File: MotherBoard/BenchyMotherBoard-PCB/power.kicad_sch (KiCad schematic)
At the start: 201 parts, among them J1 PWR-CONN, J4 UPDI-HEADER, U1 STM32MP157FAB1, U10 USB7206C, U2 TPS65400RGZT, U3 NCP51200, U4 ATTINY1606-MNR, U6 MAX15027, U7 SN74LVC1G32, U9 AP2127K-3.3

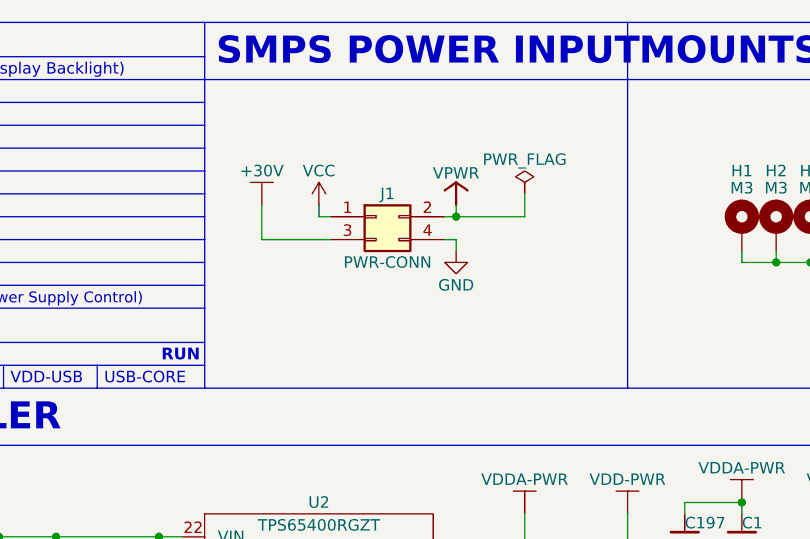
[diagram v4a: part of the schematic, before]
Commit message: Add extra functions to PMBus and create manual power sequence
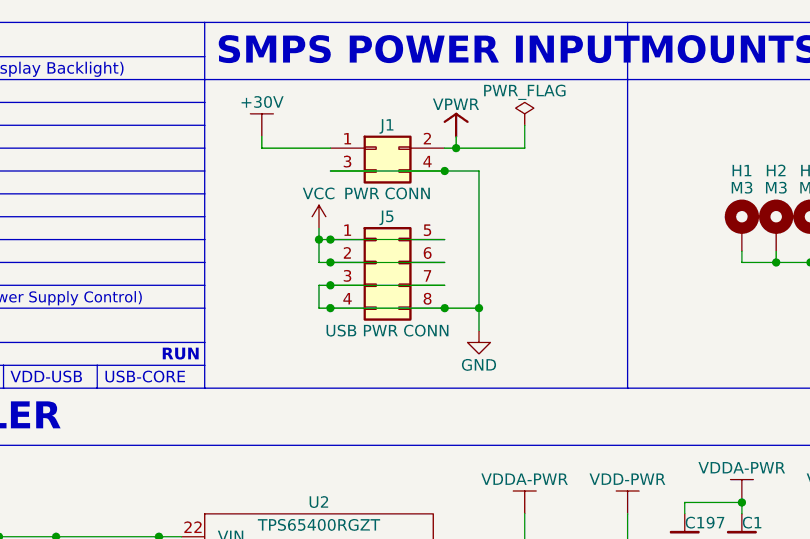
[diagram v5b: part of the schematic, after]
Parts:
- added J5: USB PWR CONN, Daxxn_Connectors:8-Pin_Molex_Mini-Fit_Jr_Vertical_Mount, symbol Connector_Generic:Conn_02x04_Top_Bottom
- J1: value PWR-CONN -> PWR CONN
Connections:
- net +30V: now also J1.1 (Pin_1); no longer J1.3 (Pin_3)
- net GND: now also J1.3 (Pin_3), J5.3 (Pin_3), J5.4 (Pin_4), J5.7 (Pin_7), J5.8 (Pin_8)
- net VCC: now also J5.1 (Pin_1), J5.2 (Pin_2), J5.5 (Pin_5), J5.6 (Pin_6); no longer J1.1 (Pin_1)
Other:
- moved on the sheet: J1

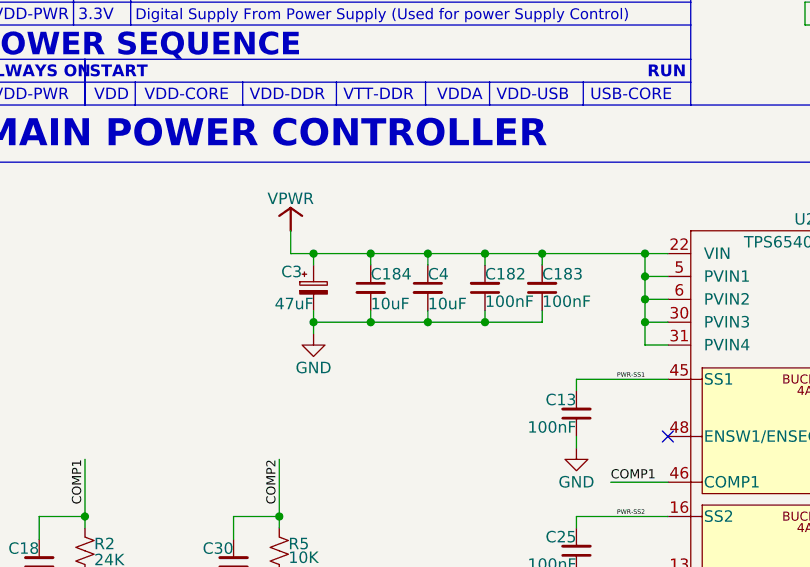
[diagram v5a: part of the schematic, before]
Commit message: Finish trace layout and update PS fb resistor values
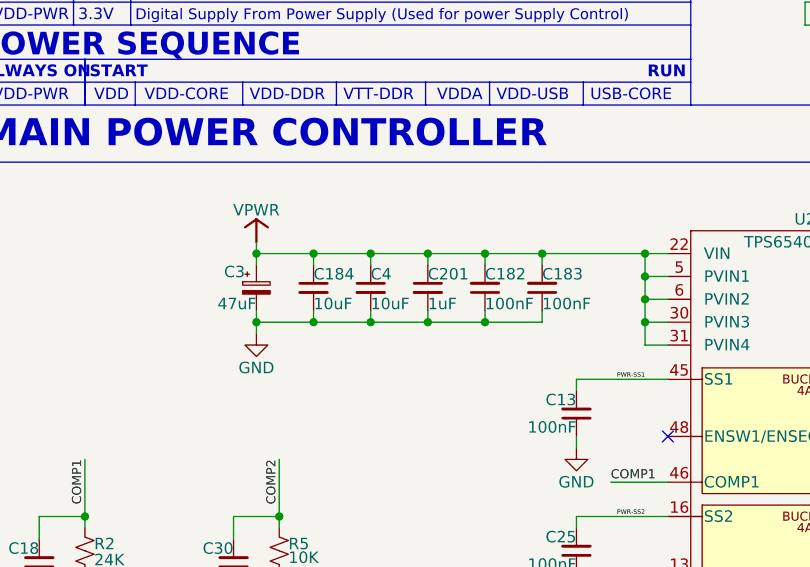
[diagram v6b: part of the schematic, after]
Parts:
- added C201: 1uF, Capacitor_SMD:C_0805_2012Metric, symbol Device:C_Small
- C3: footprint Capacitor_SMD:CP_Elec_6.3x7.7 -> Capacitor_Tantalum_SMD:CP_EIA-7343-15_Kemet-W
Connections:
- net GND: now also C201.2
- net VPWR: now also C201.1
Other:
- moved on the sheet: C184, C3, C4

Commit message: (!!WIP!!) Started schematic and block diagram
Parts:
- removed C194: 1uF, Capacitor_SMD:C_0603_1608Metric, symbol Device:C_Small
- removed C198, C71, C72, C74: 100nF, Capacitor_SMD:C_0402_1005Metric, symbol Device:C_Small
- removed D21: BZX584C3V3_R1, Diode_SMD:D_SOD-523, symbol Daxxn_Device:D_Zener
- removed J4: UPDI-HEADER, Connector_PinHeader_2.54mm:PinHeader_1x03_P2.54mm_Vertical, symbol Connector_Generic:Conn_01x03
- removed JP1: PWR-ICSP-RST, Connector_PinHeader_2.54mm:PinHeader_1x02_P2.54mm_Vertical, symbol Jumper:Jumper_2_Open
- removed R27, R41: 1K, Resistor_SMD:R_0402_1005Metric, symbol Device:R_Small_US
- removed R3, R32: 22K, Resistor_SMD:R_0402_1005Metric, symbol Device:R_Small_US
- removed R30: 10K, Resistor_SMD:R_0402_1005Metric, symbol Device:R_Small_US
- removed S1: PWR-SW, Daxxn_Switches:SW_Push_7-PR, symbol Daxxn_Buttons:GENERIC-SWITCH-2P-M
- removed S2: PWR-RESET, Daxxn_Switches:TL3365AF180QG, symbol Daxxn_Buttons:GENERIC-SWITCH-2P
- removed U1: STM32MP157FAB1, Daxxn_Packages:LFBGA354-P0.8mm-STM32MP157F, symbol Daxxn_MicroProcessors:STM32MP157FAB1
- removed U4: ATTINY1606-MNR, Daxxn_Packages:QFN-20-1EP_3x3mm_P0.4mm_EP1.5x1.5mm, symbol Daxxn_MicroControllers:ATTINY1606-MNR
- removed U7: SN74LVC1G32, Package_TO_SOT_SMD:SOT-23-5, symbol Daxxn_Logic:SN74LVC1G32
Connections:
- no-connect marks 10 -> 6
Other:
- moved on the sheet: C10, C11, C185, C186, C187, C188, C189, C19, C190, C191, C192, C193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
